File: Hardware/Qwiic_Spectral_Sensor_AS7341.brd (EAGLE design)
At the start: 31.8 x 31.8 mm, 63 parts, among them J1 QWIIC_RIGHT_ANGLE, J3 QWIIC_RIGHT_ANGLE, Q1 20V/4.2A/52mΩ/1.4W, Q2 20V/4.2A/52mΩ/1.4W, Q3 20V/4.2A/52mΩ/1.4W, U1 AS7341OLGA, U2 PCA9536, U3 AP2127K-1.8V

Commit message: Update Qwiic_Spectral_Sensor_AS7341.brd
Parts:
- moved U$21 15.9 mm to (13.0, 30.4)
- moved U$4 14.8 mm to (25.3, 30.4)
- moved U$8 5.21 mm to (20.1, 30.4)
- moved U$23 4.21 mm to (19.4, 28.8)
- moved U$3 1.28 mm to (7.62, 30.4)
- moved U$11 0.90 mm to (19.4, 30.4)
- moved U$22 0.38 mm to (12.7, 28.8)
- moved U$5 0.28 mm to (12.4, 30.4)
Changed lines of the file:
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@@
 <?xml version="1.0" encoding="utf-8"?>
 <!DOCTYPE eagle SYSTEM "eagle.dtd">
-<eagle version="9.6.2">
+<eagle version="9.5.2">
 <drawing>
 <settings>
-<setting alwaysvectorfont="no"/>
+<setting alwaysvectorfont="yes"/>
 <setting keepoldvectorfont="yes"/>
 <setting verticaltext="up"/>
@@
 <layer number="37" name="tTest" color="7" fill="1" visible="no" active="yes"/>
 <layer number="38" name="bTest" color="7" fill="1" visible="no" active="yes"/>
-<layer number="39" name="tKeepout" color="4" fill="11" visible="yes" active="yes"/>
-<layer number="40" name="bKeepout" color="1" fill="11" visible="yes" active="yes"/>
+<layer number="39" name="tKeepout" color="4" fill="11" visible="no" active="yes"/>
+<layer number="40" name="bKeepout" color="1" fill="11" visible="no" active="yes"/>
 <layer number="41" name="tRestrict" color="4" fill="10" visible="no" active="yes"/>
 <layer number="42" name="bRestrict" color="1" fill="10" visible="no" active="yes"/>
@@
 <attribute name="VALUE" x="8.89" y="-0.762" size="0.6096" layer="27" font="vector" ratio="20"/>
 </element>
-<element name="U$3" library="output" package="QWIIC0" value="" x="6.35" y="30.48" smashed="yes"/>
-<element name="U$4" library="output" package="QWIIC0" value="" x="11.43" y="35.56" smashed="yes" rot="MR0"/>
-<element name="U$5" library="output" package="SPECTRAL0" value="" x="12.7" y="30.48" smashed="yes"/>
-<element name="U$8" library="output" package="SPECTRAL0" value="" x="20.32" y="35.56" smashed="yes" rot="MR0"/>
-<element name="U$11" library="output" package="SENSOR0" value="" x="20.32" y="30.48" smashed="yes"/>
-<element name="U$21" library="output" package="SENSOR0" value="" x="27.94" y="35.56" smashed="yes" rot="MR0"/>
-<element name="U$22" library="output" package="AS73410" value="" x="12.7" y="29.21" smashed="yes"/>
-<element name="U$23" library="output" package="AS73410" value="" x="19.05" y="33.02" smashed="yes" rot="MR0"/>
+<element name="U$3" library="output" package="QWIIC0" value="" x="7.62" y="30.353" smashed="yes"/>
+<element name="U$4" library="output" package="QWIIC0" value="" x="25.273" y="30.353" smashed="yes" rot="MR0"/>
+<element name="U$5" library="output" package="SPECTRAL0" value="" x="12.446" y="30.353" smashed="yes"/>
+<element name="U$8" library="output" package="SPECTRAL0" value="" x="20.066" y="30.353" smashed="yes" rot="MR0"/>
+<element name="U$11" library="output" package="SENSOR0" value="" x="19.431" y="30.353" smashed="yes"/>
+<element name="U$21" library="output" package="SENSOR0" value="" x="12.954" y="30.353" smashed="yes" rot="MR0"/>
+<element name="U$22" library="output" package="AS73410" value="" x="12.7" y="28.829" smashed="yes"/>
+<element name="U$23" library="output" package="AS73410" value="" x="19.431" y="28.829" smashed="yes" rot="MR0"/>
 <element name="U$24" library="output" package="#GPIO#0" value="" x="22.86" y="1.778" smashed="yes" rot="R90"/>
 <element name="U$25" library="output" package="#GPIO#0" value="" x="22.86" y="1.778" smashed="yes" rot="MR90"/>

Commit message: Update Qwiic_Spectral_Sensor_AS7341.brd
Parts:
- added U$28: (no value), output:#IR#0
- added U$29: (no value), output:#WHITE#0
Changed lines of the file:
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@@
 <?xml version="1.0" encoding="utf-8"?>
 <!DOCTYPE eagle SYSTEM "eagle.dtd">
-<eagle version="9.5.2">
+<eagle version="9.6.2">
 <drawing>
 <settings>
-<setting alwaysvectorfont="yes"/>
+<setting alwaysvectorfont="no"/>
 <setting keepoldvectorfont="yes"/>
 <setting verticaltext="up"/>
@@
 <element name="U$26" library="output" package="##INT##0" value="" x="20.32" y="1.778" smashed="yes" rot="R90"/>
 <element name="U$27" library="output" package="##INT##0" value="" x="20.32" y="1.778" smashed="yes" rot="MR90"/>
+<element name="U$28" library="output" package="#IR#0" value="" x="36.83" y="21.59" smashed="yes"/>
+<element name="U$29" library="output" package="#WHITE#0" value="" x="36.83" y="24.13" smashed="yes"/>
 </elements>
 <signals>

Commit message: Update Qwiic_Spectral_Sensor_AS7341.brd
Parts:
- moved U$28 28.8 mm to (8.26, 17.8), flipped to the bottom
- moved U$29 14.8 mm to (23.5, 17.8), flipped to the bottom
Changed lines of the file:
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@@
 <?xml version="1.0" encoding="utf-8"?>
 <!DOCTYPE eagle SYSTEM "eagle.dtd">
-<eagle version="9.6.2">
+<eagle version="9.5.2">
 <drawing>
 <settings>
@@
 <element name="U$26" library="output" package="##INT##0" value="" x="20.32" y="1.778" smashed="yes" rot="R90"/>
 <element name="U$27" library="output" package="##INT##0" value="" x="20.32" y="1.778" smashed="yes" rot="MR90"/>
-<element name="U$28" library="output" package="#IR#0" value="" x="36.83" y="21.59" smashed="yes"/>
-<element name="U$29" library="output" package="#WHITE#0" value="" x="36.83" y="24.13" smashed="yes"/>
+<element name="U$28" library="output" package="#IR#0" value="" x="8.255" y="17.78" smashed="yes" rot="MR0"/>
+<element name="U$29" library="output" package="#WHITE#0" value="" x="23.495" y="17.78" smashed="yes" rot="MR0"/>
 </elements>
 <signals>

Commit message: Board review notes
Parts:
- added JP5: JUMPER-SMT_2_NC_TRACE_SILK, SparkFun-Jumpers:SMT-JUMPER_2_NC_TRACE_SILK
- added R5: 2.2k, SparkFun-Resistors:0603
- turned Q3 to 0 degrees
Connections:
- new net N$6: JP2.2, Q3.3
- net 1.8V: now also JP5.2; no longer R4.2
- net 3.3V: now also Q3.2; no longer Q3.3
- net GND: now also R5.1
- net GPIO0: now also R5.2
- net GPIO3: no longer U2.5
- net N$10: now also JP5.1, R4.2; no longer JP2.2, Q3.2
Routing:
- net GPIO0: track 19.4 -> 24.5 mm
- net N$6: track 0.00 -> 3.64 mm, vias 0 -> 1
- net 1.8V: track 22.9 -> 24.9 mm, vias 2 -> 3
- net GPIO3: track 20.3 -> 18.7 mm
- net N$10: track 3.45 -> 2.46 mm
- net GND: vias 9 -> 12

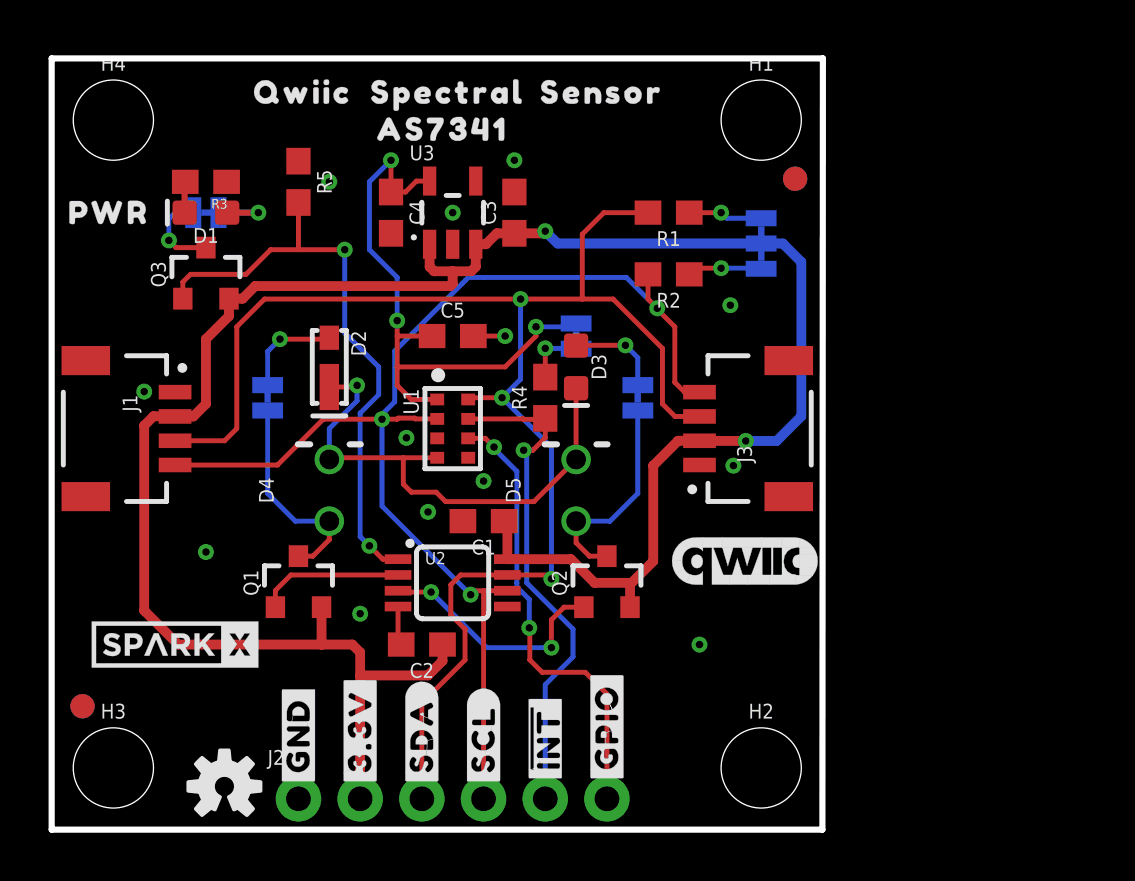
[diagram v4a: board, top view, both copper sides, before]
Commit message: Panelization
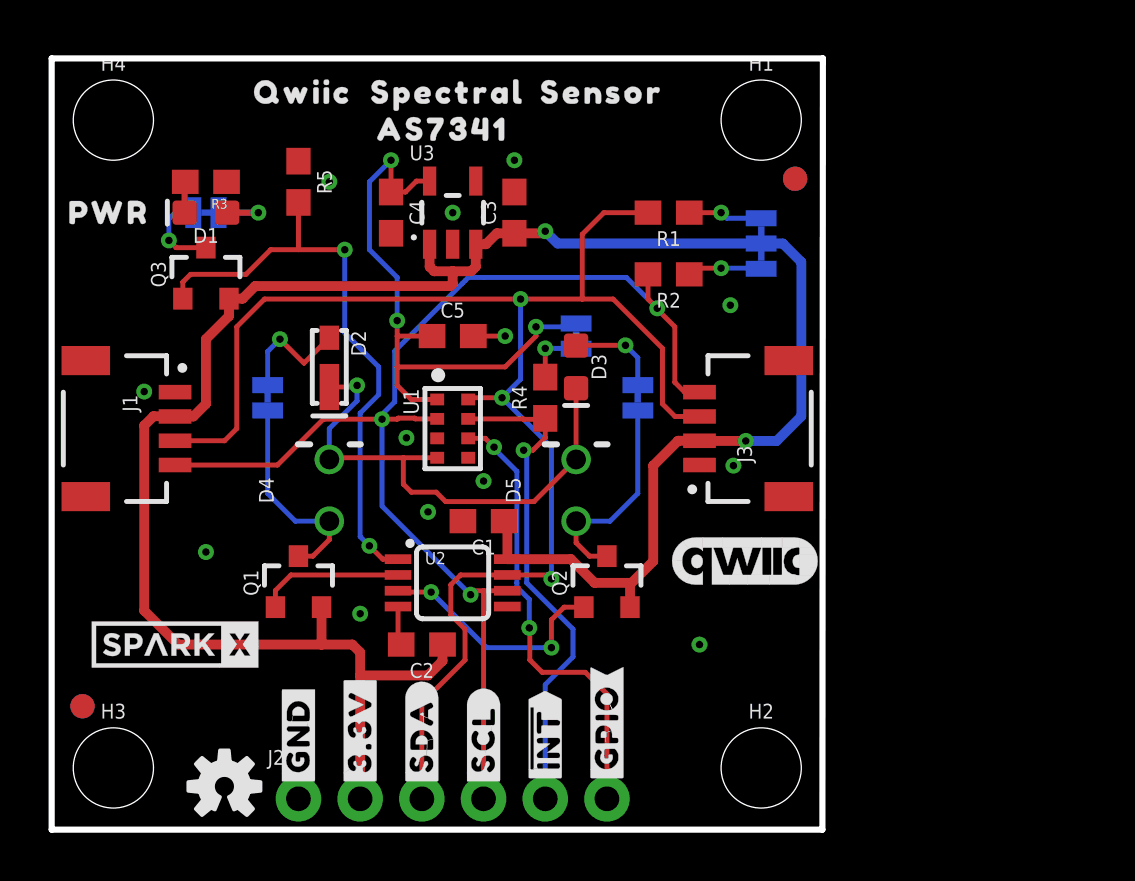
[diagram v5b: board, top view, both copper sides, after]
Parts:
- added U$30: (no value), output:##INT##0
- U$24, U$25: device output:#GPIO#0 -> output:##INT##0
- U$26, U$27: device output:##INT##0 -> output:#GPIO#0
- moved U$24 2.54 mm to (20.3, 1.78)
- moved U$25 2.54 mm to (20.3, 1.78)
- moved U$26 2.54 mm to (22.9, 1.78)
- moved U$27 2.54 mm to (22.9, 1.78)
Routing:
- net N$5: track 4.16 -> 4.98 mm
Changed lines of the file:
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@@
 <?xml version="1.0" encoding="utf-8"?>
 <!DOCTYPE eagle SYSTEM "eagle.dtd">
-<eagle version="9.5.2">
+<eagle version="9.6.2">
 <drawing>
 <settings>
-<setting alwaysvectorfont="no"/>
+<setting alwaysvectorfont="yes"/>
 <setting keepoldvectorfont="yes"/>
 <setting verticaltext="up"/>
@@
 <element name="U$22" library="output" package="AS73410" value="" x="12.7" y="28.829" smashed="yes"/>
 <element name="U$23" library="output" package="AS73410" value="" x="19.431" y="28.829" smashed="yes" rot="MR0"/>
-<element name="U$24" library="output" package="#GPIO#0" value="" x="22.86" y="1.778" smashed="yes" rot="R90"/>
-<element name="U$25" library="output" package="#GPIO#0" value="" x="22.86" y="1.778" smashed="yes" rot="MR90"/>
-<element name="U$26" library="output" package="##INT##0" value="" x="20.32" y="1.778" smashed="yes" rot="R90"/>
-<element name="U$27" library="output" package="##INT##0" value="" x="20.32" y="1.778" smashed="yes" rot="MR90"/>
 <element name="U$28" library="output" package="#IR#0" value="" x="8.255" y="17.78" smashed="yes" rot="MR0"/>
 <element name="U$29" library="output" package="#WHITE#0" value="" x="23.495" y="17.78" smashed="yes" rot="MR0"/>
@@
 <attribute name="VALUE" x="9.398" y="26.67" size="0.6096" layer="27" font="vector" ratio="20" rot="R270" align="top-center"/>
 </element>
+<element name="U$30" library="output" package="##INT##0" value="" x="20.955" y="20.32" smashed="yes" rot="MR0"/>
+<element name="U$24" library="output" package="##INT##0" value="" x="20.32" y="1.778" smashed="yes" rot="R90"/>
+<element name="U$25" library="output" package="##INT##0" value="" x="20.32" y="1.778" smashed="yes" rot="MR90"/>
+<element name="U$26" library="output" package="#GPIO#0" value="" x="22.86" y="1.778" smashed="yes" rot="R90"/>
+<element name="U$27" library="output" package="#GPIO#0" value="" x="22.86" y="1.778" smashed="yes" rot="MR90"/>
 </elements>
 <signals>
@@
 <wire x1="8.89" y1="19.685" x2="9.398" y2="20.193" width="0.2032" layer="16"/>
 <via x="9.398" y="20.193" extent="1-16" drill="0.3048"/>
-<wire x1="9.398" y1="20.193" x2="11.373" y2="20.193" width="0.2032" layer="1"/>
-<wire x1="11.373" y1="20.193" x2="11.43" y2="20.25" width="0.2032" layer="1"/>
+<wire x1="9.398" y1="20.193" x2="10.3855" y2="19.2055" width="0.2032" layer="1"/>
+<wire x1="10.3855" y1="19.2055" x2="11.43" y2="20.25" width="0.2032" layer="1"/>
 </signal>
 <signal name="N$7">

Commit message: Add schematic.
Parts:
- LOGO1: value (none) -> QWIIC_LOGO_6MM
- U$31: value (none) -> SPARKX-LOGO3
- renumbered U$2 to LOGO1, U$6 to U$31
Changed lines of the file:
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@@
 <attribute name="VALUE" x="6.35" y="26.035" size="0.6096" layer="27" font="vector" ratio="20" rot="R180" align="top-center"/>
 </element>
-<element name="U$2" library="SparkFun-Aesthetics" package="QWIIC_6MM" value="" x="28.575" y="11.049" smashed="yes"/>
 <element name="FRAME1" library="SparkFun-Aesthetics" package="CREATIVE_COMMONS" value="FRAME-LETTER" x="20.32" y="-7.62" smashed="yes">
 <attribute name="DESIGNER" value="" x="20.32" y="-7.62" size="1.778" layer="27" font="vector" ratio="15" display="off"/>
@@
 <element name="U$19" library="output" package="#SCL#0" value="" x="17.78" y="1.651" smashed="yes" rot="R90"/>
 <element name="U$20" library="output" package="#SCL#0" value="" x="17.78" y="1.651" smashed="yes" rot="MR90"/>
-<element name="U$6" library="SparkX" package="SPARKX-SMALL" value="" x="5.08" y="7.62" smashed="yes"/>
 <element name="U$7" library="SparkX" package="SPARKX-SMALL" value="" x="5.08" y="7.62" smashed="yes" rot="MR0"/>
 <element name="U1" library="AS7341" package="OLGA8" value="AS7341OLGA" x="16.51" y="16.51" smashed="yes" rot="R270">
@@
 <element name="U$26" library="output" package="#GPIO#0" value="" x="22.86" y="1.778" smashed="yes" rot="R90"/>
 <element name="U$27" library="output" package="#GPIO#0" value="" x="22.86" y="1.778" smashed="yes" rot="MR90"/>
+<element name="U$31" library="SparkX" package="SPARKX-SMALL" value="SPARKX-LOGO3" x="5.08" y="7.62" smashed="yes"/>
+<element name="LOGO1" library="SparkFun-Aesthetics" package="QWIIC_6MM" value="QWIIC_LOGO_6MM" x="28.575" y="11.049" smashed="yes"/>
 </elements>
 <signals>
